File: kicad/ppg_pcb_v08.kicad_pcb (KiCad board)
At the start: 4 copper layers, 13.5 x 13.5 mm, 26 parts, among them J1 12V, J2 GND, J3 TXP, J4 TXN, J5 RXP, J6 RXN, J7 SWDIO, J8 SWCLK, J9 NRST, U1 MAXM86161EFD+, U2 STM32C011F6U6, U3 SN65LVDS1DBVR, U4 MCP1703A-5002E/MC, U5 MCP1703A-3302E/MC, U6 SN65LVDT2DBVR

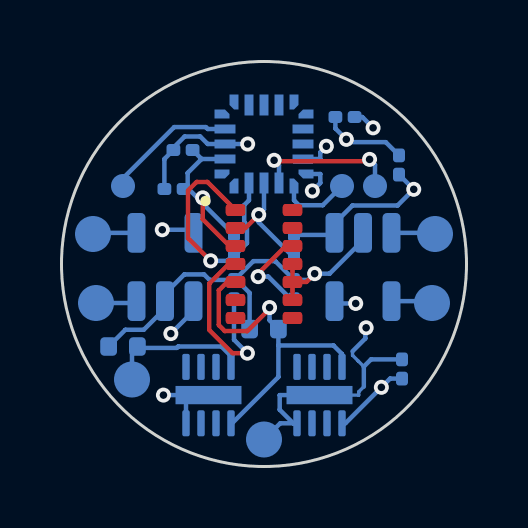
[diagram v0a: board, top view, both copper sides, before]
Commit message: Complete ESD PCB routing and validated prototype exports
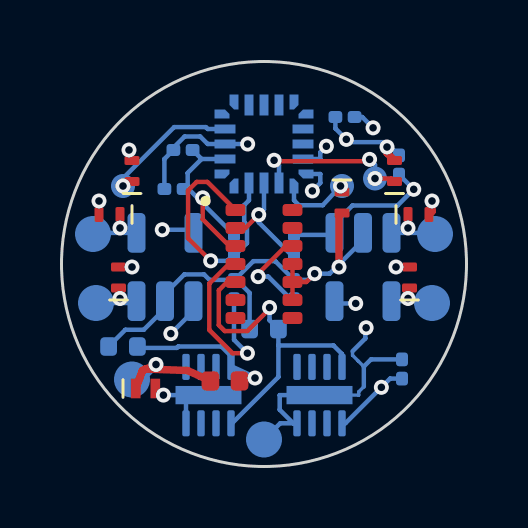
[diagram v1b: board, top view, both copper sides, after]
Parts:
- added D1: SPHV15-01ETG, SleepBud:TVS_SOD882_1x0.6, F.Cu at (-3.95, 4.15)
- added D2: ESD351DPYR, SleepBud:TI_DPY0002A_1x0.6, F.Cu at (4.85, 0.45)
- added D3: ESD351DPYR, SleepBud:TI_DPY0002A_1x0.6, F.Cu at (5.15, -1.65)
- added D4: ESD351DPYR, SleepBud:TI_DPY0002A_1x0.6, F.Cu at (-4.85, 0.45)
- added D5: ESD351DPYR, SleepBud:TI_DPY0002A_1x0.6, F.Cu at (-5.15, -1.65)
- added D6: ESD351DPYR, SleepBud:TI_DPY0002A_1x0.6, F.Cu at (2.60, -2.05)
- added D7: ESD351DPYR, SleepBud:TI_DPY0002A_1x0.6, F.Cu at (4.35, -3.10)
- added D8: ESD351DPYR, SleepBud:TI_DPY0002A_1x0.6, F.Cu at (-4.40, -3.10)
- added FB1: BLM15PX601SN1D, Inductor_SMD:L_0402_1005Metric, F.Cu at (-1.30, 3.90)
- C1, C13: footprint C_0402_1005Metric -> Capacitor_SMD:C_0402_1005Metric
- C11, C12, C14, C4, C5, C6, C7: footprint C_0201_0603Metric -> Capacitor_SMD:C_0201_0603Metric
- R1, R2: footprint R_0201_0603Metric -> Resistor_SMD:R_0201_0603Metric
- U2: footprint ST_UFQFPN-20_3x3mm_P0.5mm -> Package_DFN_QFN:ST_UFQFPN-20_3x3mm_P0.5mm
- U3, U6: footprint SOT-23-5 -> Package_TO_SOT_SMD:SOT-23-5
- U4, U5: footprint DFN-8-1EP_2x3mm_P0.5mm_EP0.61x2.2mm -> Package_DFN_QFN:DFN-8-1EP_2x3mm_P0.5mm_EP0.61x2.2mm
- moved J8 0.25 mm to (3.70, -2.85)
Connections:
- net NRST renamed /NRST
- net RXN renamed /RXN
- net RXP renamed /RXP
- net SCL renamed /SCL
- net SDA renamed /SDA
- net SWCLK renamed /SWCLK
- net SWDIO renamed /SWDIO
- net TXN renamed /TXN
- net TXP renamed /TXP
- net UART_RX renamed /UART_RX
- net UART_TX renamed /UART_TX
- net VLDO renamed /VLDO
- net VREF renamed /VREF
- J1 pad 1: 12V -> /12V_IN
- U1 pad 13: (no net) -> unconnected-(U1-GPIO-Pad13)
- U1 pad 14: (no net) -> unconnected-(U1-INTB-Pad14)
- U1 pad 6: (no net) -> unconnected-(U1-NC-Pad6)
- U1 pad 7: (no net) -> unconnected-(U1-NC-Pad7)
- U1 pad 8: (no net) -> unconnected-(U1-NC-Pad8)
- U2 pad 1: (no net) -> unconnected-(U2-PC15-Pad1)
- U2 pad 10: (no net) -> unconnected-(U2-PA5-Pad10)
- U2 pad 11: (no net) -> unconnected-(U2-PA6-Pad11)
- U2 pad 12: (no net) -> unconnected-(U2-PA7-Pad12)
- U2 pad 13: (no net) -> unconnected-(U2-PA8-Pad13)
- U2 pad 20: (no net) -> unconnected-(U2-PC14-Pad20)
- U2 pad 5: (no net) -> unconnected-(U2-PA0-Pad5)
- U2 pad 6: (no net) -> unconnected-(U2-PA1-Pad6)
- U2 pad 7: (no net) -> unconnected-(U2-PA2-Pad7)
- U2 pad 8: (no net) -> unconnected-(U2-PA3-Pad8)
- U2 pad 9: (no net) -> unconnected-(U2-PA4-Pad9)
- U4 pad 2: (no net) -> unconnected-(U4-NC-Pad2)
- U4 pad 3: (no net) -> unconnected-(U4-NC-Pad3)
- U4 pad 5: (no net) -> unconnected-(U4-NC-Pad5)
- U4 pad 6: (no net) -> unconnected-(U4-NC-Pad6)
- U4 pad 7: (no net) -> unconnected-(U4-NC-Pad7)
- U5 pad 2: (no net) -> unconnected-(U5-NC-Pad2)
- U5 pad 3: (no net) -> unconnected-(U5-NC-Pad3)
- U5 pad 5: (no net) -> unconnected-(U5-NC-Pad5)
- U5 pad 6: (no net) -> unconnected-(U5-NC-Pad6)
- U5 pad 7: (no net) -> unconnected-(U5-NC-Pad7)
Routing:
- net /12V_IN: track 0.00 -> 5.14 mm, vias 0 -> 1
- net GND: track 33.9 -> 38.9 mm, vias 5 -> 12
- net /SWCLK: track 5.01 -> 5.95 mm, vias 2 -> 3
- net /TXN: track 1.47 -> 2.08 mm, vias 0 -> 1
- net /RXN: track 1.47 -> 2.08 mm, vias 0 -> 1
- net /RXP: track 1.38 -> 1.90 mm, vias 0 -> 1
- net /TXP: track 1.38 -> 1.83 mm, vias 0 -> 1
- net /NRST: track 4.39 -> 4.75 mm, vias 0 -> 1
- net 12V: track 4.83 -> 5.09 mm, vias 0 -> 1
- net /SWDIO: track 2.34 -> 2.52 mm, vias 0 -> 1
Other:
- board text added: "J1"
- board text added: "J2"
- board text added: "J3"
- board text added: "J4"
- board text added: "J5"
- board text added: "J6"
- board text added: "J7"
- board text added: "J8"
- board text added: "J9"
- board text removed: "12V"
- board text removed: "GND"
- board text removed: "NRST"
- board text removed: "RXN"
- board text removed: "RXP"
- board text removed: "SWCLK"
- board text removed: "SWDIO"
- board text removed: "TXN"
- board text removed: "TXP"
